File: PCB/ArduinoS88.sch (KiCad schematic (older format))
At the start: 20 parts, among them J1 S88 Output, J2 S88 Input, J3 AVR-ISP-6, J4 Screw_Terminal_01x03, J5 Screw_Terminal_01x03, J6 Screw_Terminal_01x03, J7 Screw_Terminal_01x03, J8 Screw_Terminal_01x03, J9 Screw_Terminal_01x02, U1 ATmega8-16PU

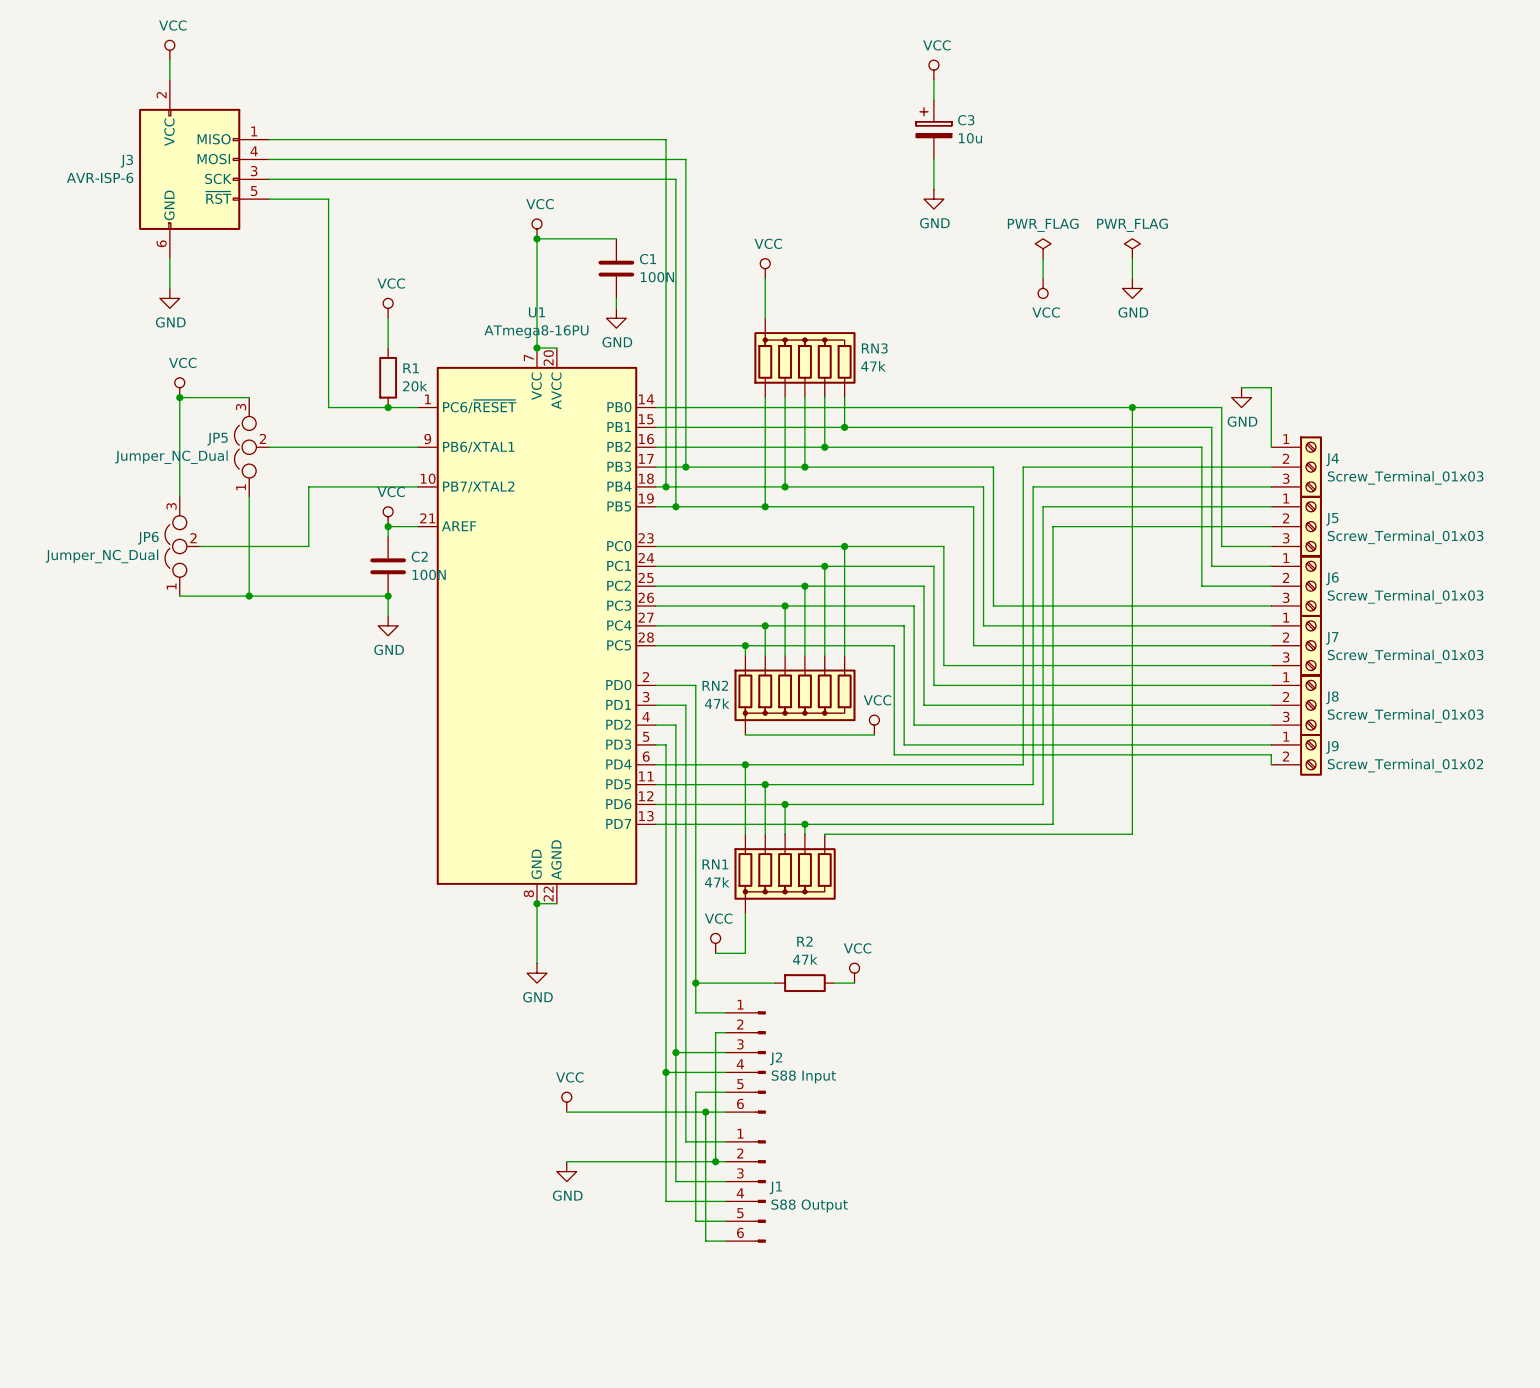
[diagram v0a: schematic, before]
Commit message: Updated connectors and added Gerber files
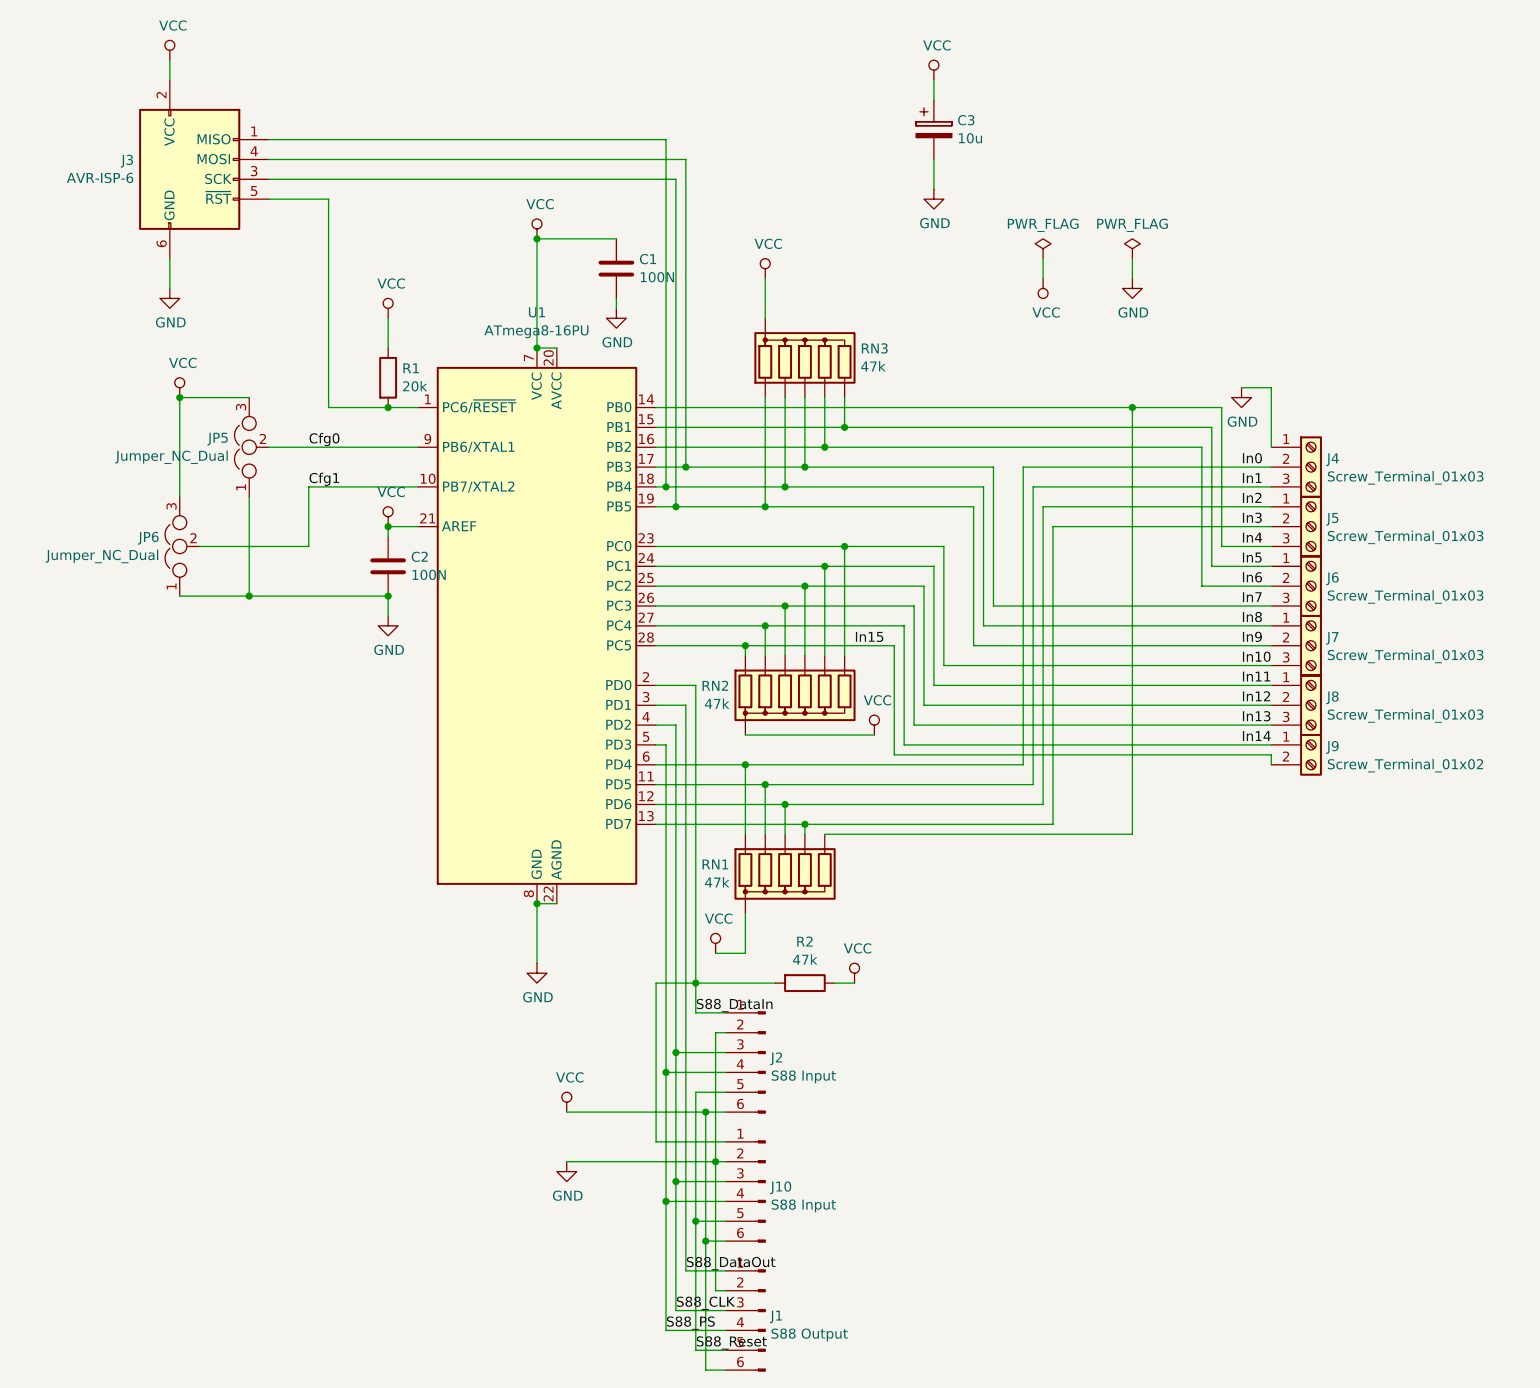
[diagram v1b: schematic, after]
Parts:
- added J10: S88 Input, Connector_Molex:Molex_KK-254_AE-6410-06A_1x06_P2.54mm_Vertical, symbol Connector:Conn_01x06_Male
- J1: footprint Connector_Molex:Molex_KK-254_AE-6410-06A_1x06_P2.54mm_Vertical -> Connector_PinHeader_2.54mm:PinHeader_1x06_P2.54mm_Horizontal
- J2: footprint Connector_Molex:Molex_KK-254_AE-6410-06A_1x06_P2.54mm_Vertical -> Connector_PinSocket_2.54mm:PinSocket_1x06_P2.54mm_Horizontal
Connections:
- net GND: now also J10.2 (Pin_2)
- net VCC: now also J10.6 (Pin_6)
- net Cfg1: now reaches JP6.2, U1.10 (PB7/XTAL2)
- net In1: now reaches J4.3 (Pin_3), RN1.3 (R2), U1.11 (PD5)
- net In2: now reaches J5.1 (Pin_1), RN1.4 (R3), U1.12 (PD6)
- net In3: now reaches J5.2 (Pin_2), RN1.5 (R4), U1.13 (PD7)
- net In4: now reaches J5.3 (Pin_3), RN1.6 (R5), U1.14 (PB0)
- net In5: now reaches J6.1 (Pin_1), RN3.6 (R5), U1.15 (PB1)
- net In6: now reaches J6.2 (Pin_2), RN3.5 (R4), U1.16 (PB2)
- net In7: now reaches J3.4 (MOSI), J6.3 (Pin_3), RN3.4 (R3), U1.17 (PB3)
- net In8: now reaches J3.1 (MISO), J7.1 (Pin_1), RN3.3 (R2), U1.18 (PB4)
- net In9: now reaches J3.3 (SCK), J7.2 (Pin_2), RN3.2 (R1), U1.19 (PB5)
- net S88_DataIn: now reaches J2.1 (Pin_1), R2.2, U1.2 (PD0)
- net S88_DataIn: now also J10.1 (Pin_1)
- net In10: now reaches J7.3 (Pin_3), RN2.7 (R6), U1.23 (PC0)
- net In11: now reaches J8.1 (Pin_1), RN2.6 (R5), U1.24 (PC1)
- net In12: now reaches J8.2 (Pin_2), RN2.5 (R4), U1.25 (PC2)
- net In13: now reaches J8.3 (Pin_3), RN2.4 (R3), U1.26 (PC3)
- net In14: now reaches J9.1 (Pin_1), RN2.3 (R2), U1.27 (PC4)
- net In15: now reaches J9.2 (Pin_2), RN2.2 (R1), U1.28 (PC5)
- net S88_DataOut: now reaches J1.1 (Pin_1), U1.3 (PD1)
- net S88_CLK: now reaches J1.3 (Pin_3), J2.3 (Pin_3), U1.4 (PD2)
- net S88_CLK: now also J10.3 (Pin_3)
- net S88_PS: now reaches J1.4 (Pin_4), J2.4 (Pin_4), U1.5 (PD3)
- net S88_PS: now also J10.4 (Pin_4)
- net In0: now reaches J4.2 (Pin_2), RN1.2 (R1), U1.6 (PD4)
- net Cfg0: now reaches JP5.2, U1.9 (PB6/XTAL1)
- net S88_Reset: now reaches J1.5 (Pin_5), J2.5 (Pin_5)
- net S88_Reset: now also J10.5 (Pin_5)
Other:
- moved on the sheet: J1
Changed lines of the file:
@@
 EESchema Schematic File Version 4
-LIBS:CANSwitchboard-cache
+LIBS:ArduinoS88-cache
 EELAYER 26 0
 EELAYER END
@@
 F 0 "J2" H 6322 5673 50  0000 R CNN
 F 1 "S88 Input" H 6322 5582 50  0000 R CNN
-F 2 "Connector_Molex:Molex_KK-254_AE-6410-06A_1x06_P2.54mm_Vertical" H 6350 5700 50  0001 C CNN
+F 2 "Connector_PinSocket_2.54mm:PinSocket_1x06_P2.54mm_Horizontal" H 6350 5700 50  0001 C CNN
 F 3 "~" H 6350 5700 50  0001 C CNN
 	1    6350 5700
@@
 L Connector:Conn_01x06_Male J1
 U 1 1 5C2E8645
-P 6350 6350
-F 0 "J1" H 6323 6323 50  0000 R CNN
-F 1 "S88 Output" H 6323 6232 50  0000 R CNN
-F 2 "Connector_Molex:Molex_KK-254_AE-6410-06A_1x06_P2.54mm_Vertical" H 6350 6350 50  0001 C CNN
-F 3 "~" H 6350 6350 50  0001 C CNN
-	1    6350 6350
+P 6350 7000
+F 0 "J1" H 6323 6973 50  0000 R CNN
+F 1 "S88 Output" H 6323 6882 50  0000 R CNN
+F 2 "Connector_PinHeader_2.54mm:PinHeader_1x06_P2.54mm_Horizontal" H 6350 7000 50  0001 C CNN
+F 3 "~" H 6350 7000 50  0001 C CNN
+	1    6350 7000
 	-1   0    0    -1
 $EndComp
@@
 Wire Wire Line
 	6100 5600 6100 6250
-Connection ~ 6100 6250
-Wire Wire Line
-	6100 6250 6150 6250
-Wire Wire Line
-	6050 6000 6050 6650
-Wire Wire Line
-	6050 6650 6150 6650
 Connection ~ 6050 6000
 Wire Wire Line
@@
 	5800 3950 5950 3950
 Wire Wire Line
-	5950 3950 5950 6150
-Wire Wire Line
-	5950 6150 6150 6150
-Wire Wire Line
-	6000 5900 6000 6550
-Wire Wire Line
 	6000 5900 6150 5900
 Wire Wire Line
-	6000 6550 6150 6550
-Wire Wire Line
 	5900 4050 5900 5700
 Wire Wire Line
@@
 Wire Wire Line
 	5800 4050 5900 4050
-Wire Wire Line
-	5900 5700 5900 6350
-Wire Wire Line
-	5900 6350 6150 6350
 Connection ~ 5900 5700
 Wire Wire Line
@@
 Wire Wire Line
 	5850 5800 6150 5800
-Wire Wire Line
-	5850 5800 5850 6450
-Wire Wire Line
-	5850 6450 6150 6450
 Connection ~ 5850 5800
 $Comp
@@
 	1    0    0    -1
 $EndComp
+$Comp
+L Connector:Conn_01x06_Male J10
+U 1 1 5C2E0B83
+P 6350 6350
+F 0 "J10" H 6322 6323 50  0000 R CNN
+F 1 "S88 Input" H 6322 6232 50  0000 R CNN
+F 2 "Connector_Molex:Molex_KK-254_AE-6410-06A_1x06_P2.54mm_Vertical" H 6350 6350 50  0001 C CNN
+F 3 "~" H 6350 6350 50  0001 C CNN
+	1    6350 6350
+	-1   0    0    -1
+$EndComp
+Wire Wire Line
+	5850 7100 6150 7100
+Wire Wire Line
+	5850 5800 5850 6450
+Wire Wire Line
+	5950 6800 6150 6800
+Wire Wire Line
+	5950 3950 5950 6800
+Wire Wire Line
+	6100 6250 6100 6900
+Wire Wire Line
+	6100 6900 6150 6900
+Connection ~ 6100 6250
+Wire Wire Line
+	6100 6250 6150 6250
+Wire Wire Line
+	5900 7000 6150 7000
+Wire Wire Line
+	5900 5700 5900 6350
+Wire Wire Line
+	6000 7200 6150 7200
+Wire Wire Line
+	6000 5900 6000 6550
+Wire Wire Line
+	6050 7300 6150 7300
+Wire Wire Line
+	6050 6000 6050 6650
+Wire Wire Line
+	6150 6650 6050 6650
+Connection ~ 6050 6650
+Wire Wire Line
+	6050 6650 6050 7300
+Wire Wire Line
+	6150 6550 6000 6550
+Connection ~ 6000 6550
+Wire Wire Line
+	6000 6550 6000 7200
+Wire Wire Line
+	6150 6450 5850 6450
+Connection ~ 5850 6450
+Wire Wire Line
+	5850 6450 5850 7100
+Wire Wire Line
+	6150 6350 5900 6350
+Connection ~ 5900 6350
+Wire Wire Line
+	5900 6350 5900 7000
+Wire Wire Line
+	6000 5350 5800 5350
+Wire Wire Line
+	5800 5350 5800 6150
+Wire Wire Line
+	5800 6150 6150 6150
+Text Label 8750 2750 0    50   ~ 0
+In0
+Text Label 8750 2850 0    50   ~ 0
+In1
+Text Label 8750 2950 0    50   ~ 0
+In2
+Text Label 8750 3050 0    50   ~ 0
+In3
+Text Label 8750 3150 0    50   ~ 0
+In4
+Text Label 8750 3250 0    50   ~ 0
+In5
+Text Label 8750 3350 0    50   ~ 0
+In6
+Text Label 8750 3450 0    50   ~ 0
+In7
+Text Label 8750 3550 0    50   ~ 0
+In8
+Text Label 8750 3650 0    50   ~ 0
+In9
+Text Label 8750 3750 0    50   ~ 0
+In10
+Text Label 8750 3850 0    50   ~ 0
+In11
+Text Label 8750 3950 0    50   ~ 0
+In12
+Text Label 8750 4050 0    50   ~ 0
+In13
+Text Label 8750 4150 0    50   ~ 0
+In14
+Text Label 6800 3650 0    50   ~ 0
+In15
+Text Label 6000 7200 0    50   ~ 0
+S88_Reset
+Text Label 5850 7100 0    50   ~ 0
+S88_PS
+Text Label 5900 7000 0    50   ~ 0
+S88_CLK
+Text Label 5950 6800 0    50   ~ 0
+S88_DataOut
+Text Label 6000 5500 0    50   ~ 0
+S88_DataIn
+Text Label 4050 2650 0    50   ~ 0
+Cfg0
+Text Label 4050 2850 0    50   ~ 0
+Cfg1
 $EndSCHEMATC
